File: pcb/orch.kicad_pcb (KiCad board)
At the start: 2 copper layers, 313.6 x 80.8 mm, 147 parts, among them J1 AVR-ISP-6, P1 USB_C_Receptacle_USB2.0, SW1 MX-NoLED, SW10 MX-NoLED, SW11 MX-NoLED, SW12 MX-NoLED, SW13 MX-NoLED, SW14 MX-NoLED, SW15 MX-NoLED, SW16 MX-NoLED, SW17 MX-NoLED, SW18 MX-NoLED, SW19 MX-NoLED, SW2 MX-NoLED, SW20 MX-NoLED, SW21 MX-NoLED, SW22 MX-NoLED, SW23 MX-NoLED, SW24 MX-NoLED, SW25 MX-NoLED, SW26 MX-NoLED, SW27 MX-NoLED, SW28 MX-NoLED, SW29 MX-NoLED, SW3 MX-NoLED, SW30 MX-NoLED, SW31 MX-NoLED, SW32 MX-NoLED, SW33 MX-NoLED, SW34 MX-NoLED, SW35 MX-NoLED, SW36 MX-NoLED, SW37 MX-NoLED, SW38 MX-NoLED, SW39 MX-NoLED, SW4 MX-NoLED, SW40 MX-NoLED, SW41 MX-NoLED, SW42 MX-NoLED, SW43 MX-NoLED, SW44 MX-NoLED, SW45 MX-NoLED, SW46 MX-NoLED, SW47 MX-NoLED, SW48 MX-NoLED, SW49 MX-NoLED, SW5 MX-NoLED, SW50 MX-NoLED, SW51 MX-NoLED, SW52 MX-NoLED, SW53 MX-NoLED, SW54 MX-NoLED, SW55 Rotary_Encoder_Switch, SW56 MX-NoLED, SW57 MX-NoLED, SW58 MX-NoLED, SW59 MX-NoLED, SW6 MX-NoLED, SW60 MX-NoLED, SW61 Reset, SW7 MX-NoLED, SW8 MX-NoLED, SW9 MX-NoLED, U1 ATmega32U4-AU, Y1 16MHz

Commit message: fix caps for leds
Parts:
- added C10: 0.1u, Capacitor_SMD:C_0805_2012Metric_Pad1.15x1.40mm_HandSolder, B.Cu at (202.4, 117.6)
- added C11: 0.1u, Capacitor_SMD:C_0805_2012Metric_Pad1.15x1.40mm_HandSolder, B.Cu at (107.4, 117.6)
- added C12: 0.1u, Capacitor_SMD:C_0805_2012Metric_Pad1.15x1.40mm_HandSolder, B.Cu at (107.2, 161.0)
- added C13: 0.1u, Capacitor_SMD:C_0805_2012Metric_Pad1.15x1.40mm_HandSolder, B.Cu at (202.4, 161.0)
- added C14: 0.1u, Capacitor_SMD:C_0805_2012Metric_Pad1.15x1.40mm_HandSolder, B.Cu at (298.2, 161.0)
- added C9: 0.1u, Capacitor_SMD:C_0805_2012Metric_Pad1.15x1.40mm_HandSolder, B.Cu at (306.9, 117.6)
- moved D66 11.3 mm to (298.2, 156.7), turned to 180 degrees
- moved D65 2.44 mm to (202.4, 156.7), turned to 180 degrees
- moved D64 2.42 mm to (107.2, 156.7), turned to 180 degrees
- moved D62 0.69 mm to (202.4, 121.8)
- moved D63 0.69 mm to (107.4, 121.8)
- moved D61 0.63 mm to (306.9, 121.8)
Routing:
- net +5V: track 590.0 -> 640.6 mm, vias 9 -> 11
- net GND: track 112.9 -> 132.4 mm
- net Net-(D65-Pad4): track 112.8 -> 94.0 mm
- net Net-(D64-Pad4): track 102.3 -> 92.3 mm
- net Net-(D63-Pad4): track 48.5 -> 38.9 mm
- net Net-(D61-Pad4): track 100.9 -> 103.8 mm
- net Net-(D62-Pad4): track 91.4 -> 94.3 mm

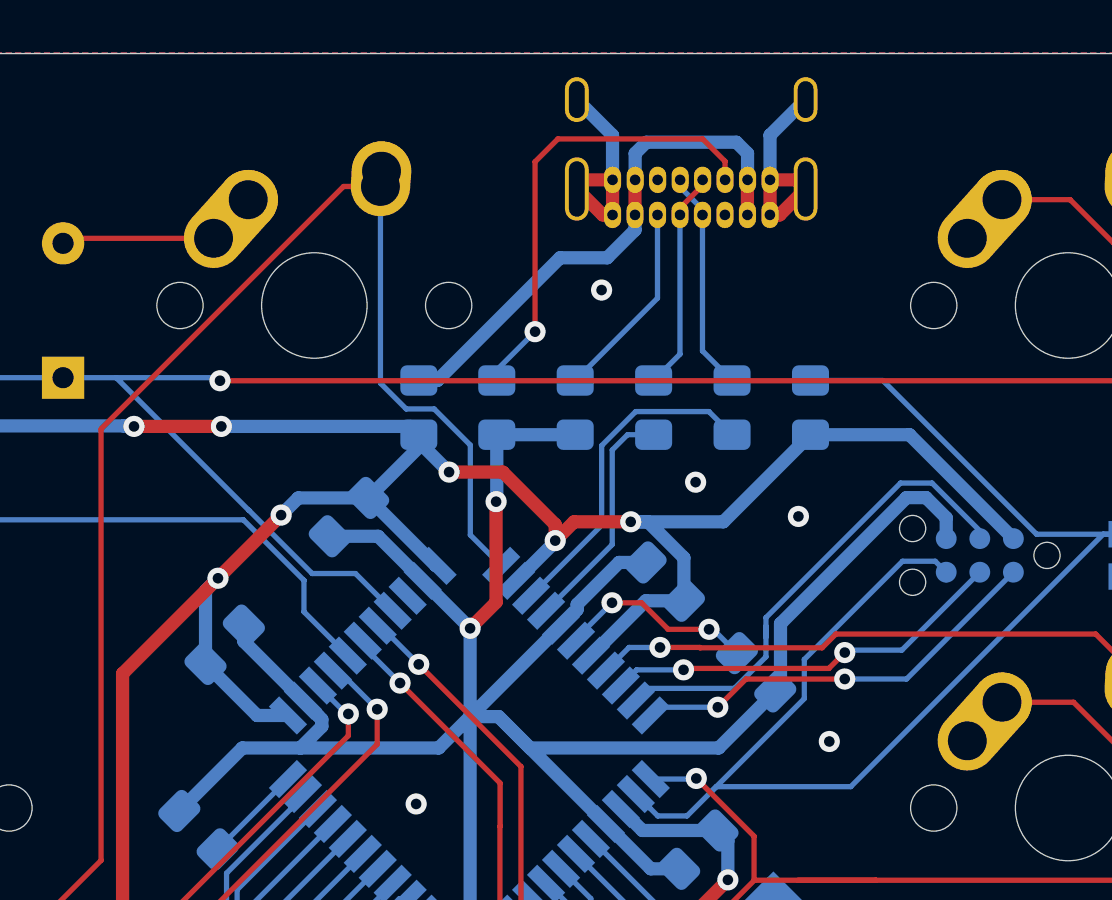
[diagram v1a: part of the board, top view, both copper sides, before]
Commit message: v2.1 - add caps to LEDs, re-do some routing
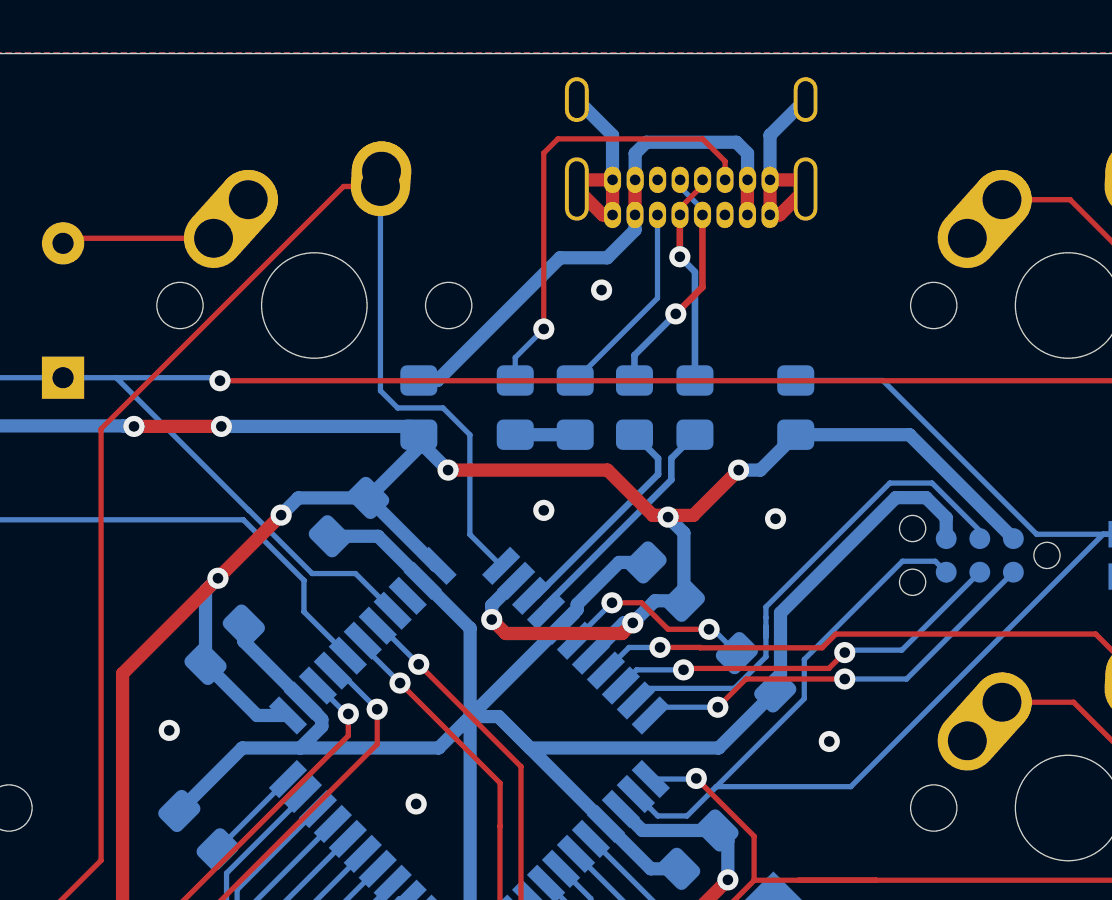
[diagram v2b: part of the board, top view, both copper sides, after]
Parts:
- moved R2 1.40 mm to (345.1, 115.5)
- moved R3 0.72 mm to (342.8, 115.5)
- moved R5 0.70 mm to (338.3, 115.5)
- moved R1 0.56 mm to (348.9, 115.5)
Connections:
- R2 pad 1: /D- -> /D+
- R2 pad 2: Net-(P1-PadA7) -> Net-(P1-PadA6)
- R3 pad 1: /D+ -> /D-
- R3 pad 2: Net-(P1-PadA6) -> Net-(P1-PadA7)
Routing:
- net GND: track 132.4 -> 124.2 mm, vias 37 -> 36
- net +5V: track 640.6 -> 645.0 mm, vias 11 -> 13
- net /D-: track 12.6 -> 8.57 mm
- net Net-(P1-PadA7): track 8.40 -> 9.04 mm, vias 0 -> 1
- net /Reset: track 56.0 -> 56.5 mm
- net Net-(P1-PadA6): track 8.35 -> 8.18 mm, vias 0 -> 1
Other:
- net class USB added: clearance 0.2, trace_width 0.7, via_dia 0.8, via_drill 0.4
- board text added: "orch v2.1"
- board text removed: "orch v2"

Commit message: bump out usb connector
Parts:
- moved P1 3.00 mm to (345.0, 99.1)
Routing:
- net Net-(P1-PadA6): track 8.18 -> 11.3 mm
- net Net-(F1-Pad2): track 20.4 -> 23.4 mm
- net Net-(P1-PadA5): track 7.55 -> 10.6 mm
- net Net-(P1-PadA7): track 9.04 -> 12.0 mm
- net Net-(P1-PadB5): track 17.2 -> 20.1 mm
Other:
- board size 313.6 x 80.8 mm -> 313.6 x 83.8 mm

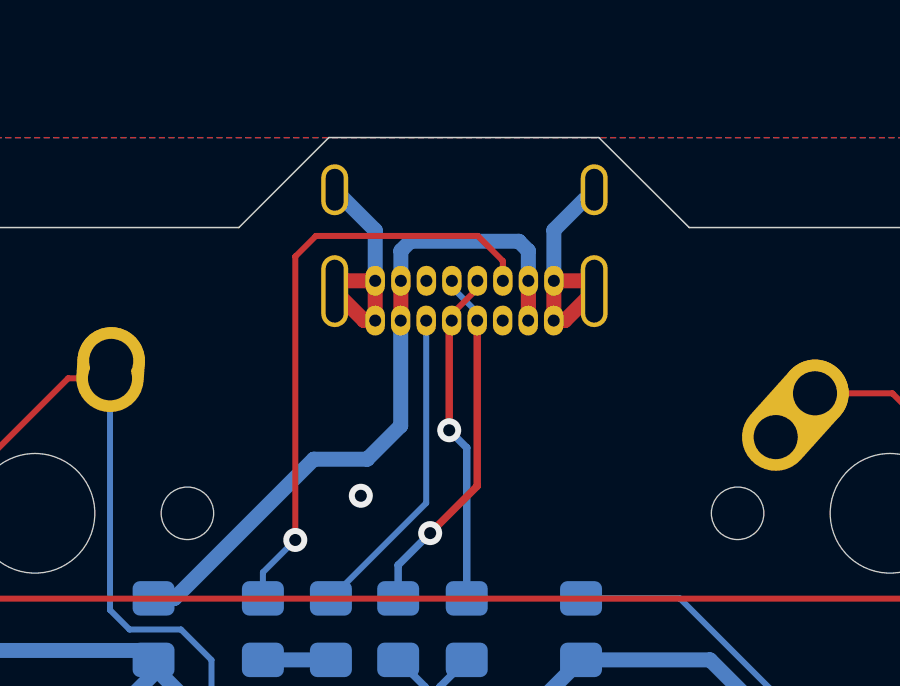
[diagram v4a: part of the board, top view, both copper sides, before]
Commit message: flip usb
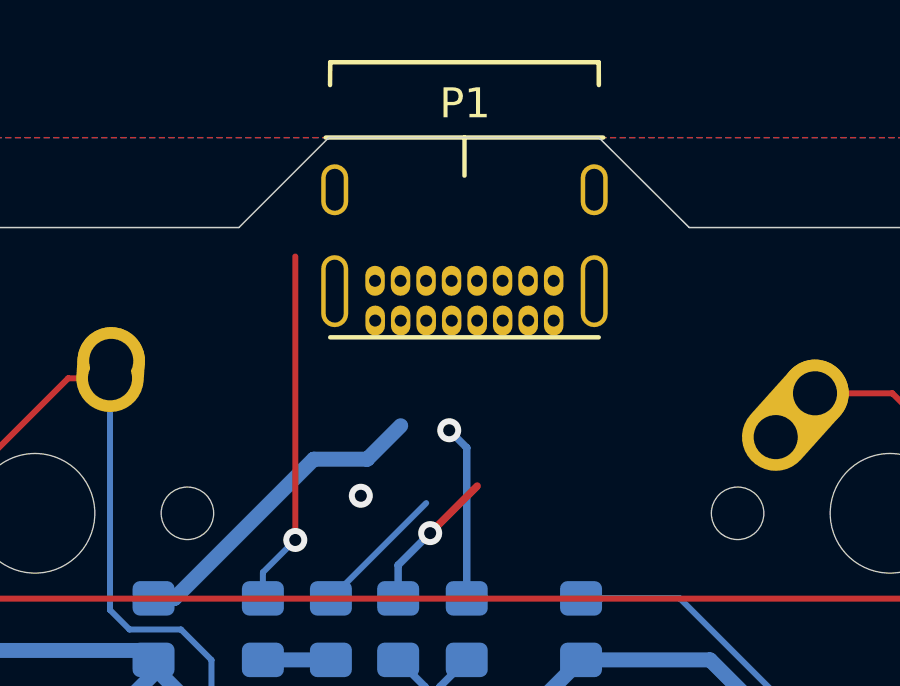
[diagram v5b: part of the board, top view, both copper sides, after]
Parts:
- P1: moved to F.Cu
- turned P1 to 180 degrees
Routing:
- net GND: track 124.2 -> 107.8 mm
- net Net-(F1-Pad2): track 23.4 -> 10.7 mm
- net Net-(P1-PadB5): track 20.1 -> 11.8 mm
- net Net-(P1-PadA7): track 12.0 -> 5.52 mm
- net Net-(P1-PadA5): track 10.6 -> 4.49 mm
- net Net-(P1-PadA6): track 11.3 -> 6.33 mm

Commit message: flip
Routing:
- net GND: track 107.8 -> 124.2 mm
- net Net-(F1-Pad2): track 10.7 -> 23.4 mm
- net Net-(P1-PadB5): track 11.8 -> 17.7 mm
- net Net-(P1-PadA5): track 4.49 -> 0.00 mm
- net Net-(P1-PadA6): track 6.33 -> 2.16 mm, vias 1 -> 0
- net Net-(P1-PadA7): track 5.52 -> 2.36 mm, vias 1 -> 0

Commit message: 3.0
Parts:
- added C14: 0.1u, Capacitor_SMD:C_0805_2012Metric_Pad1.18x1.45mm_HandSolder, B.Cu at (246.3, 161.0)
- added C15: 0.1u, Capacitor_SMD:C_0805_2012Metric_Pad1.18x1.45mm_HandSolder, B.Cu at (329.7, 167.1)
- added D67: SK6812, LED_SMD:LED_SK6812_PLCC4_5.0x5.0mm_P3.2mm, B.Cu at (246.3, 156.7)
- added D68: SK6812, LED_SMD:LED_SK6812_PLCC4_5.0x5.0mm_P3.2mm, B.Cu at (329.7, 162.8)
- C1, C2, C3, C4, C5, C6, C7: footprint Capacitor_SMD:C_0805_2012Metric_Pad1.15x1.40mm_HandSolder -> Capacitor_SMD:C_0805_2012Metric_Pad1.18x1.45mm_HandSolder
- C10: renamed from C11; footprint Capacitor_SMD:C_0805_2012Metric_Pad1.15x1.40mm_HandSolder -> Capacitor_SMD:C_0805_2012Metric_Pad1.18x1.45mm_HandSolder
- C11: renamed from C12; footprint Capacitor_SMD:C_0805_2012Metric_Pad1.15x1.40mm_HandSolder -> Capacitor_SMD:C_0805_2012Metric_Pad1.18x1.45mm_HandSolder
- C12: renamed from C13; footprint Capacitor_SMD:C_0805_2012Metric_Pad1.15x1.40mm_HandSolder -> Capacitor_SMD:C_0805_2012Metric_Pad1.18x1.45mm_HandSolder
- C13: renamed from C14; footprint Capacitor_SMD:C_0805_2012Metric_Pad1.15x1.40mm_HandSolder -> Capacitor_SMD:C_0805_2012Metric_Pad1.18x1.45mm_HandSolder
- C16: renamed from C8; footprint Capacitor_SMD:C_0805_2012Metric_Pad1.15x1.40mm_HandSolder -> Capacitor_SMD:C_0805_2012Metric_Pad1.18x1.45mm_HandSolder
- C8: renamed from C9; footprint Capacitor_SMD:C_0805_2012Metric_Pad1.15x1.40mm_HandSolder -> Capacitor_SMD:C_0805_2012Metric_Pad1.18x1.45mm_HandSolder
- C9: renamed from C10; footprint Capacitor_SMD:C_0805_2012Metric_Pad1.15x1.40mm_HandSolder -> Capacitor_SMD:C_0805_2012Metric_Pad1.18x1.45mm_HandSolder
- P1: moved to B.Cu
- moved G*** 162.0 mm to (239.4, 177.2)
- moved C13 148.4 mm to (149.8, 161.0)
- moved D66 148.4 mm to (149.8, 156.7)
- moved C12 113.8 mm to (88.6, 161.0)
- moved D65 113.8 mm to (88.6, 156.7)
- moved C11 47.2 mm to (88.6, 117.6), turned to 0 degrees
- moved C9 43.9 mm to (246.3, 117.6)
- moved D62 43.9 mm to (246.3, 121.8)
- moved C10 42.4 mm to (149.8, 117.6)
- moved D63 42.4 mm to (149.8, 121.8)
- moved D64 39.5 mm to (88.6, 121.8), turned to 0 degrees
- moved C8 14.5 mm to (321.4, 117.6)
- moved D61 14.5 mm to (321.4, 121.8)
- moved R3 2.41 mm to (343.9, 113.3), turned to 0 degrees
- moved R2 1.20 mm to (343.9, 115.6), turned to 0 degrees
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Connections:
- net Net-(P1-PadA6) renamed /USB_D+
- net Net-(P1-PadA7) renamed /USB_D-
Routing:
- net +5V: track 645.0 -> 743.5 mm
- net Net-(D66-Pad4): track 0.00 -> 93.4 mm
- net Net-(D67-Pad4): track 0.00 -> 79.9 mm
- net Net-(D64-Pad4): track 92.3 -> 37.9 mm, vias 0 -> 2
- net Net-(D65-Pad4): track 94.0 -> 59.6 mm
- net Net-(D61-Pad4): track 103.8 -> 74.4 mm
- net Net-(D63-Pad4): track 38.9 -> 60.5 mm, vias 2 -> 0
- net /RGB: track 26.9 -> 11.0 mm
- net Net-(P1-PadA5): track 0.00 -> 10.6 mm
- net /USB_D+: track 2.16 -> 12.7 mm
- net /USB_D-: track 2.36 -> 10.1 mm
- net /D-: track 8.57 -> 11.4 mm
- net Net-(P1-PadB5): track 17.7 -> 19.8 mm
- net Net-(D62-Pad4): track 94.3 -> 95.8 mm
- net Net-(F1-Pad2): track 23.4 -> 22.4 mm
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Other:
- board text added: "orch v3.0"
- board text removed: "orch v2.1"
